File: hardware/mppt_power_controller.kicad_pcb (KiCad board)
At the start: 2 copper layers, 100 x 50 mm, 60 parts, among them J1 Solar Input, J2 USB_B_Micro, J3 Conn_ARM_JTAG_SWD_10, J4 Battery, J5 Curiosity Board, Q1 Q_NMOS_GSD, Q2 Q_NMOS_GSD, U1 INA233, U2 PX3519, U3 ATSAMD21G18A-AUT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

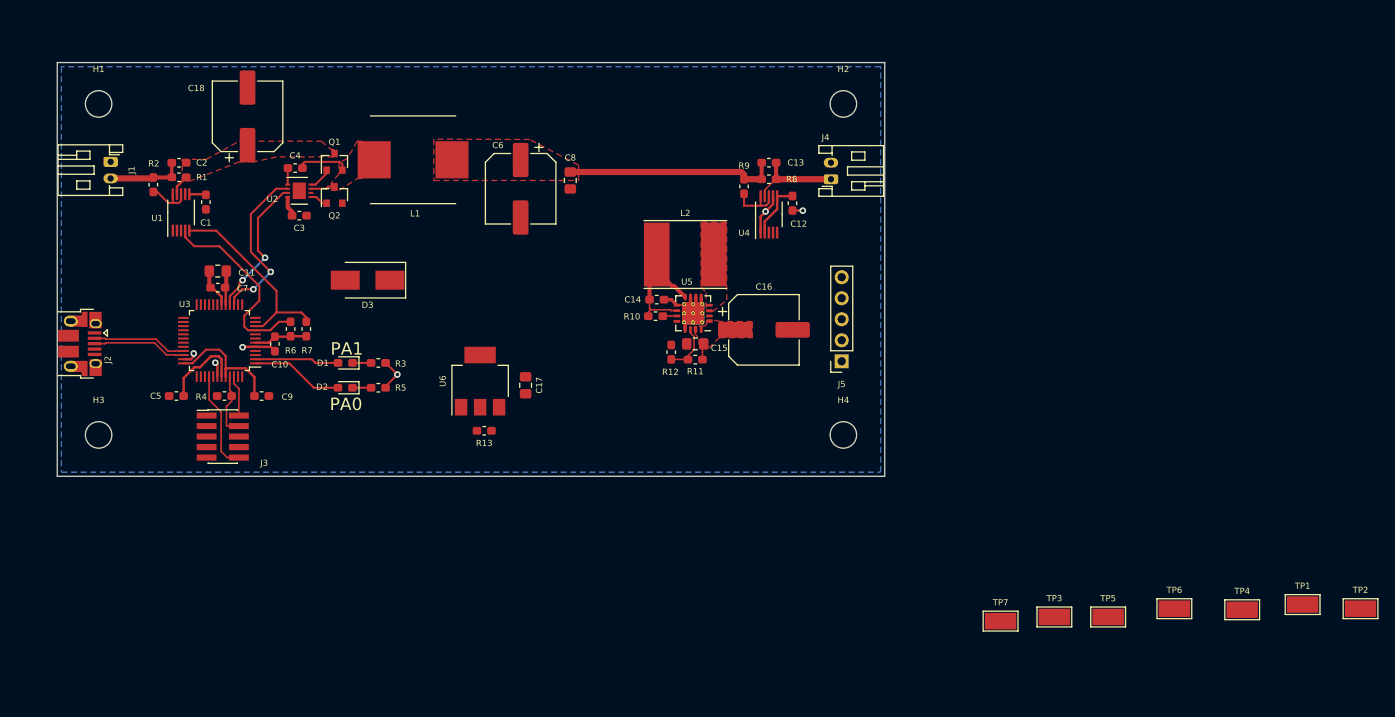
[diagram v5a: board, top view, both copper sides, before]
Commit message: Move around 5V SMPS
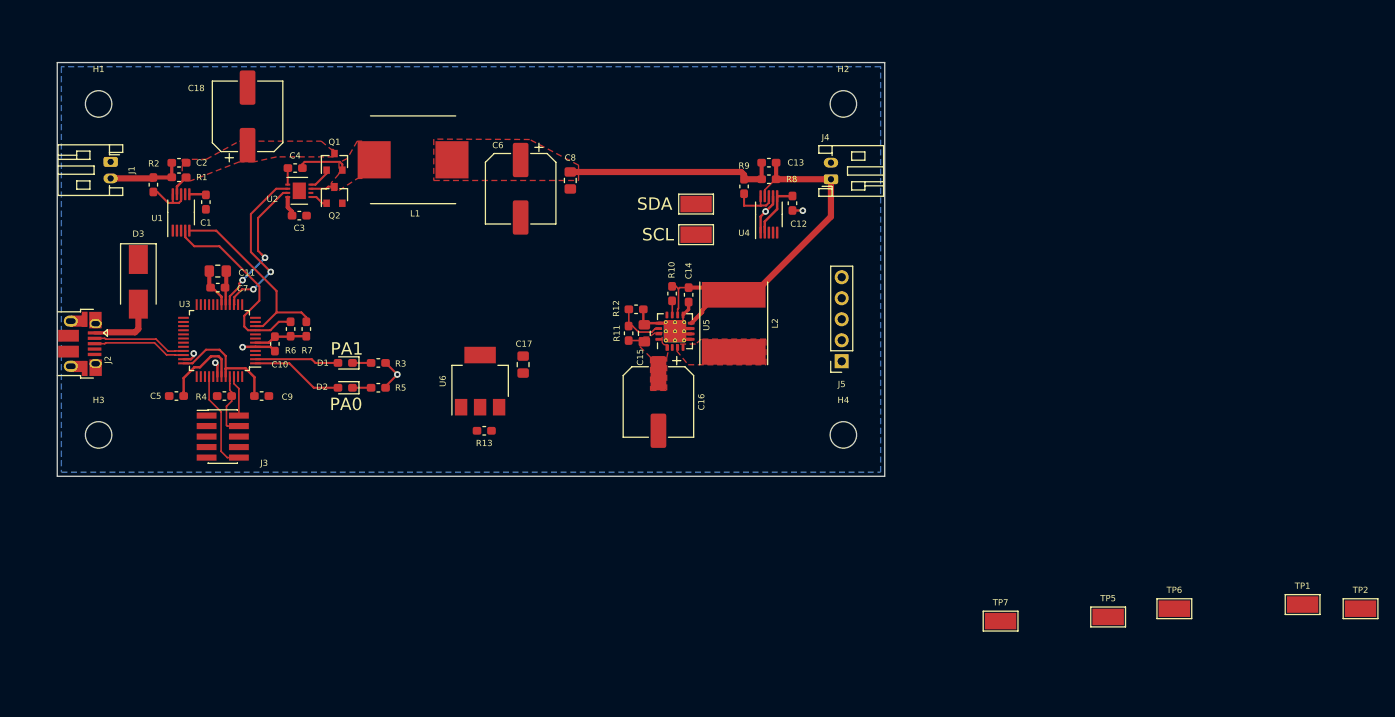
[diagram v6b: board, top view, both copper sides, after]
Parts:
- removed TP3: SDA, TestPoint:TestPoint_Keystone_5019_Minature
- removed TP4: SCL, TestPoint:TestPoint_Keystone_5019_Minature
- added SCL: SCL, TestPoint:TestPoint_Keystone_5019_Minature, F.Cu at (147.2, 80.8)
- added SDA: SDA, TestPoint:TestPoint_Keystone_5019_Minature, F.Cu at (147.2, 77.1)
- moved D3 27.7 mm to (79.8, 86.5), turned to -90 degrees
- moved C16 15.4 mm to (142.7, 101.0), turned to -90 degrees
- moved L2 10.2 mm to (151.8, 91.5), turned to -90 degrees
- moved R11 8.66 mm to (139.1, 92.7), turned to 90 degrees
- moved R12 6.70 mm to (139.9, 89.8), turned to 0 degrees
- moved C15 6.28 mm to (140.9, 92.7), turned to 90 degrees
- moved C14 3.89 mm to (146.3, 88.1), turned to -90 degrees
- moved R10 3.38 mm to (144.3, 87.9), turned to -90 degrees
- moved U5 3.09 mm to (144.7, 92.5), turned to 90 degrees
- moved C17 2.52 mm to (126.3, 96.5)
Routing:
- net /VBat: track 29.2 -> 49.4 mm
- net /Vusb: track 0.00 -> 8.48 mm
- net GND: track 33.2 -> 36.9 mm

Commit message: Add a test point for VBat. Route rest of power, I2C, test points, and everything else! Lots of cleanup needed from here to make the board look nice, but all of the nets have been routed.
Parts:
- added TP8: Battery, TestPoint:TestPoint_Keystone_5019_Minature, F.Cu at (156.8, 68.0)
- moved TP1 149.4 mm to (82.2, 68.8)
- moved TP2 134.5 mm to (99.5, 84.6)
- moved TP6 79.8 mm to (129.8, 99.4)
- moved TP5 74.8 mm to (129.8, 94.0)
- moved TP7 58.8 mm to (129.8, 104.8)
- moved J5 12.4 mm to (165.3, 83.8), turned to 0 degrees
- moved C17 11.4 mm to (116.1, 101.5), turned to 90 degrees
- moved R13 11.0 mm to (120.8, 93.5), turned to 180 degrees
- moved U6 1.02 mm to (121.3, 99.5), turned to -90 degrees
- renumbered SDA to TP3, SCL to TP4
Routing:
- net /3.3V: track 34.3 -> 217.4 mm, vias 0 -> 4
- net /5V: track 4.35 -> 125.8 mm, vias 0 -> 4
- net /SDA: track 24.0 -> 103.6 mm, vias 0 -> 4
- net /SCL: track 23.8 -> 99.9 mm, vias 0 -> 2
- net GND: track 36.9 -> 107.2 mm, vias 6 -> 29
- net Net-(C2-Pad2): track 9.23 -> 14.5 mm
- net /VBat: track 49.4 -> 53.6 mm
- net /FET_PWM: track 20.3 -> 24.3 mm
- net Net-(R13-Pad1): track 0.00 -> 3.65 mm
- added copper zone on F.Cu, net GND
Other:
- rule trace_min: 0.2 -> 0.13
- board text added: "Solar MPPT Buck Power Supply Jon Neal, Nov 2019 EECE 4038C"

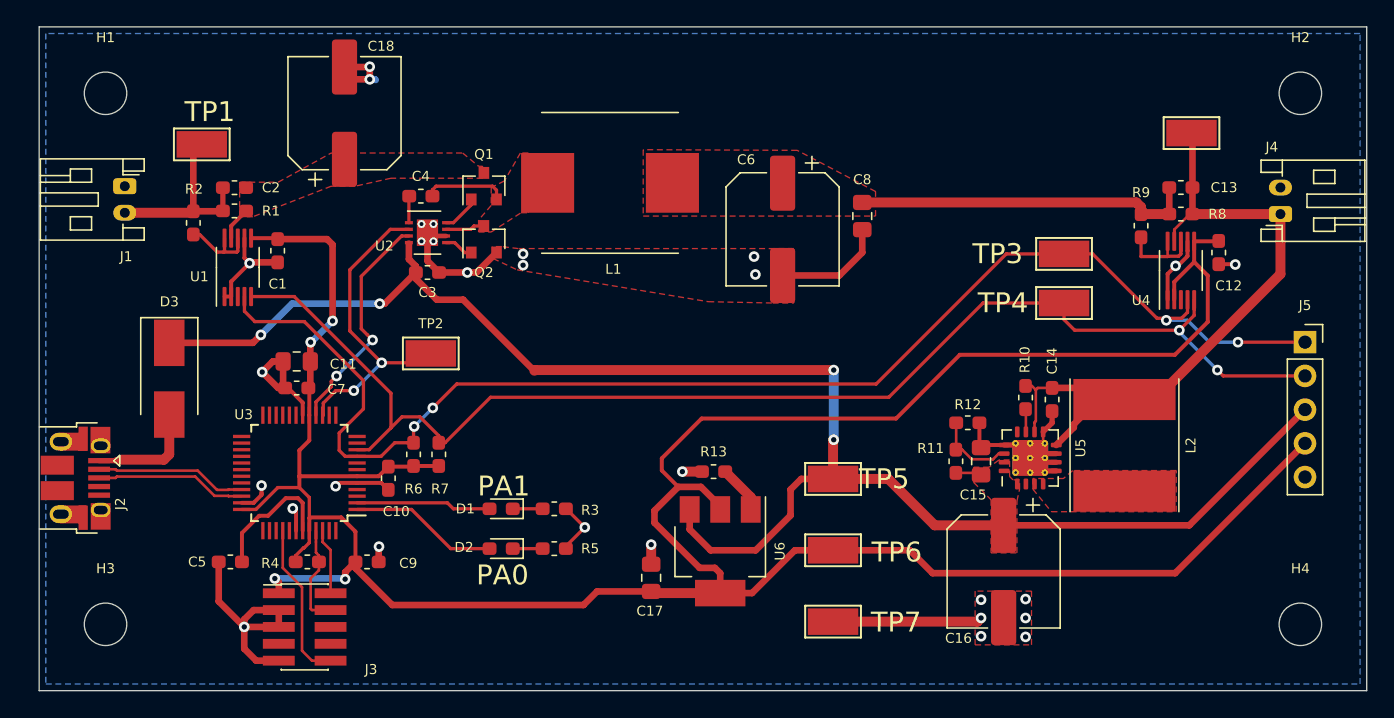
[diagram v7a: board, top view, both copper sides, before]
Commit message: Remove test point reference designators. Also labelled some of the different circuits on the PCB.
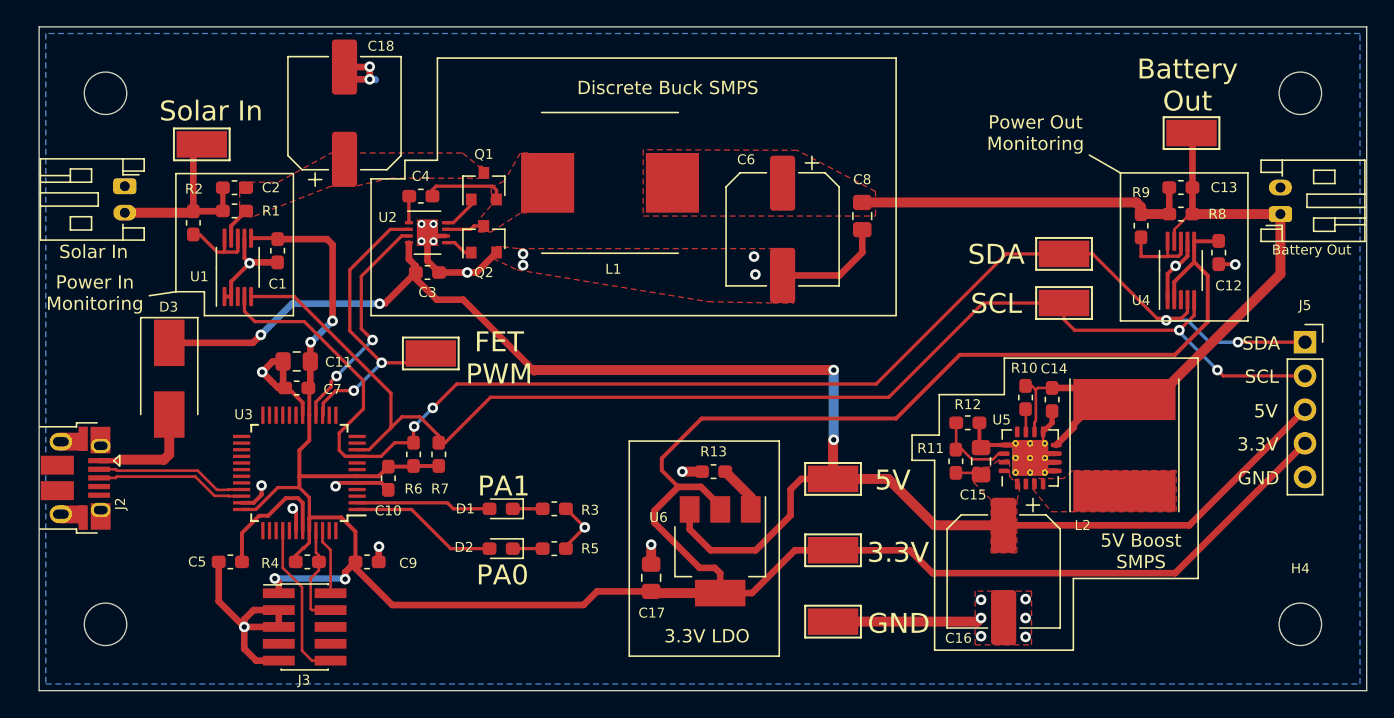
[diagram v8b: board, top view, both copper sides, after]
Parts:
- Battery Out: renamed from J4
- Solar In: renamed from J1
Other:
- board text added: "3.3V"
- board text added: "3.3V LDO"
- board text added: "5V"
- board text added: "5V Boost SMPS"
- board text added: "Battery Out"
- board text added: "Discrete Buck SMPS"
- board text added: "FET PWM"
- board text added: "GND"
- board text added: "Power In Monitoring"
- board text added: "Power Out Monitoring"
- board text added: "SCL"
- board text added: "SDA"
- board text added: "Solar In"
